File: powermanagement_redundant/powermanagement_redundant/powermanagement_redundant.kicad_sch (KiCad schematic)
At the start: 3 parts, among them K1 SISF00DN-T1-GE3, K2 SISF00DN-T1-GE3

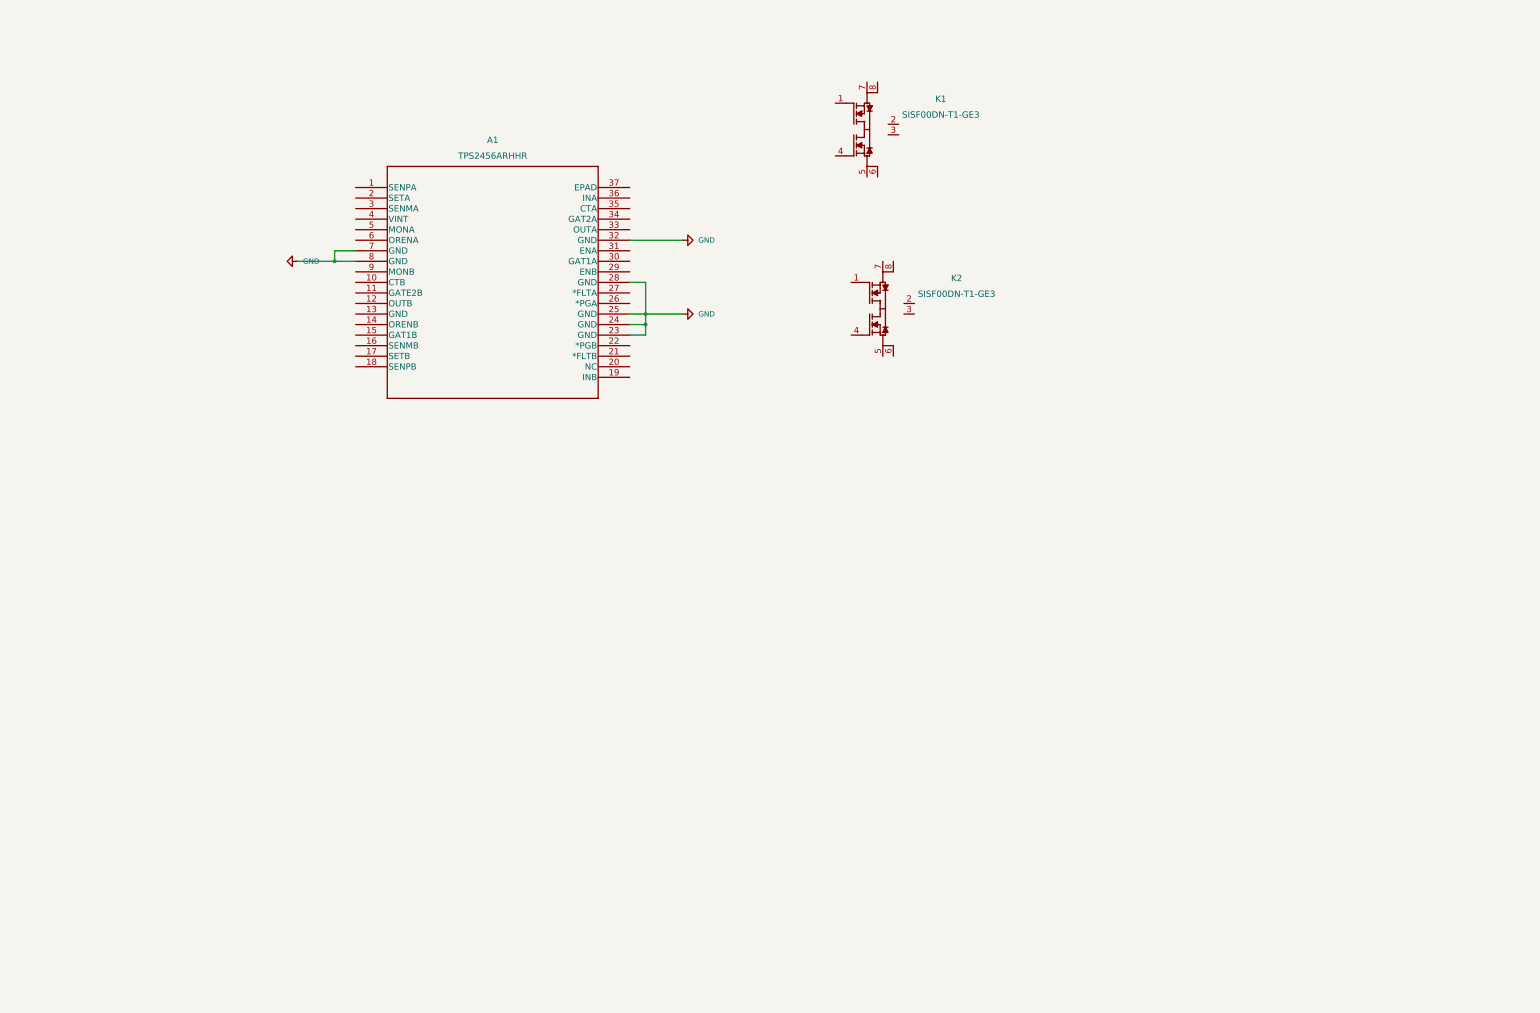
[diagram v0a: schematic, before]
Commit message: Bauteileplatzierung Fertig!
Alle Bauteile sind jetzt alle platziert. Werte die bereits Bekannt sind hab ich auch eingetragen. Berechnung der Bauteile erfolgt demnächst.
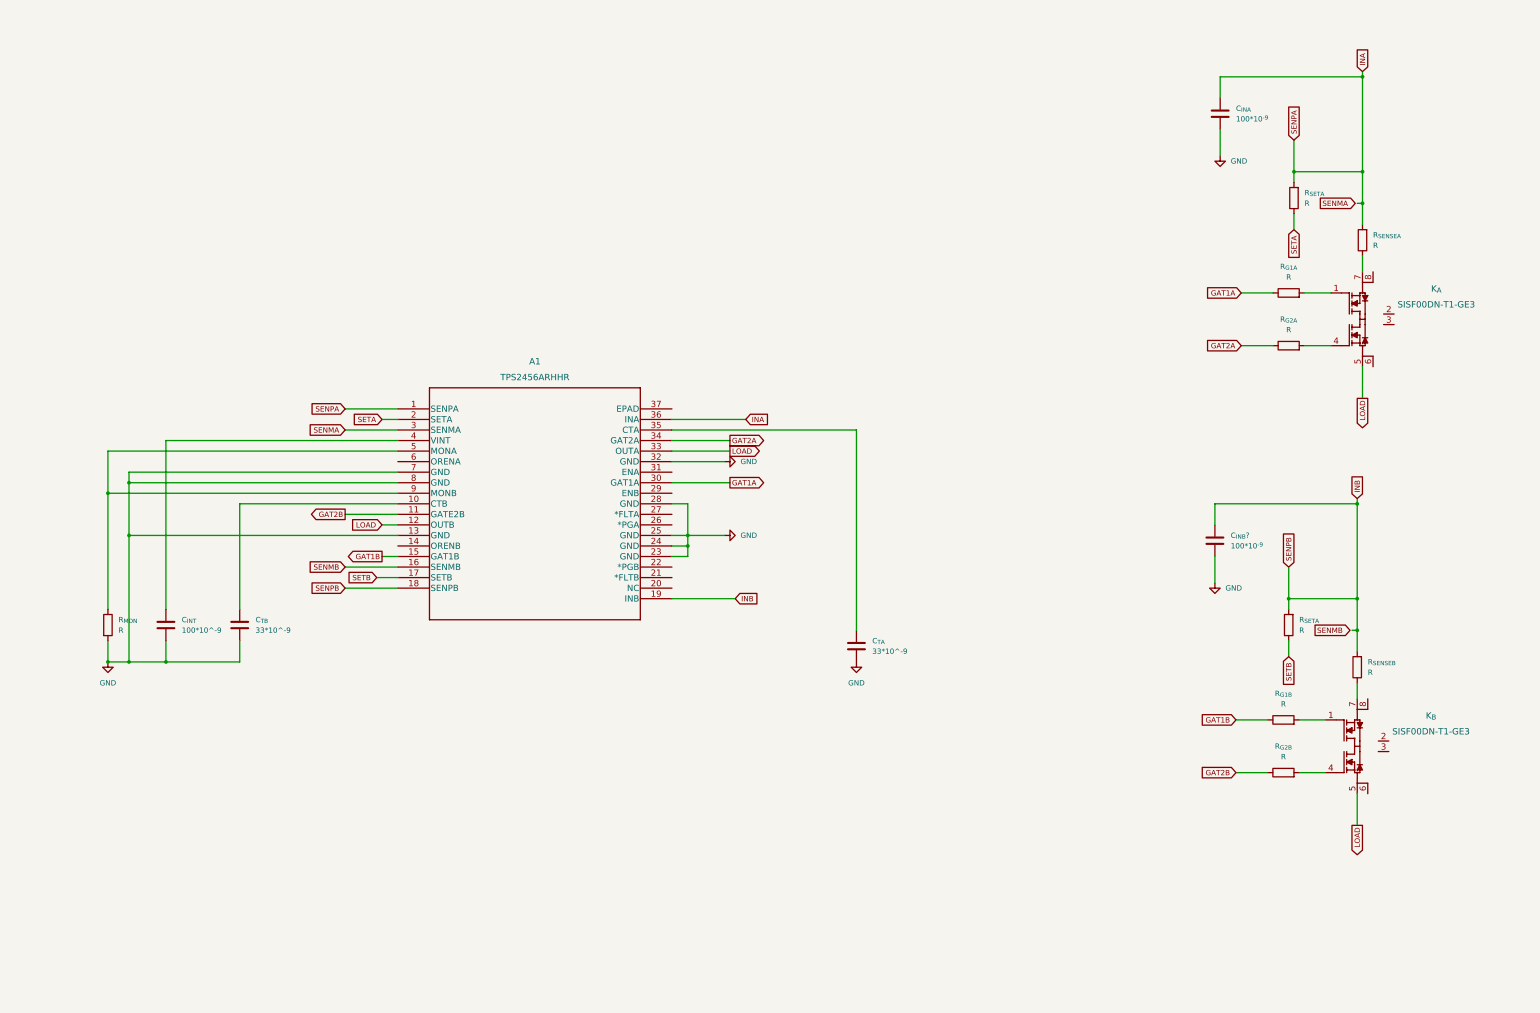
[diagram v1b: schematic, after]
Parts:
- removed K2: SISF00DN-T1-GE3, SISF00DN-1:SISF00DN-T1-GE3, symbol SISF00DN-T1:SISF00DN-T1-GE3
- added C_{INA}, C_{INB}?: 100*10^{-9}, symbol Device:C
- added C_{INT}: 100*10^-9, symbol Device:C
- added C_{TA}, C_{TB}: 33*10^-9, symbol Device:C
- added K_{B}: SISF00DN-T1-GE3, SISF00DN-1:SISF00DN-T1-GE3, symbol SISF00DN-T1:SISF00DN-T1-GE3
- added R_{G1A}, R_{G1B}, R_{G2A}, R_{G2B}, R_{MON}, R_{SENSEA}, R_{SENSEB}, R_{SETA} (x2): R, symbol Device:R
- renumbered K1 to K_{A}
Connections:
- net GND: now also A1.13 (GND), C_{INA}.2, C_{INB}?.2, C_{INT}.2, C_{TA}.2, C_{TB}.2, R_{MON}.2
- net at K_{A}.1 (G1): now also R_{G1A}.2
- net at K_{A}.4 (G2): now also R_{G2A}.2
- net LOAD: now reaches K_{A}.5 (S2)
- net LOAD: now also A1.12 (OUTB), A1.33 (OUTA), K_{B}.5 (S2)
- net at K_{A}.7 (S1): now also R_{SENSEA}.1
- net INA: now reaches A1.1 (SENPA)
- net INA: now also A1.36 (INA), C_{INA}.1, R_{SENSEA}.2, R_{SETA}.2
- net at A1.10 (CTB): now also C_{TB}.1
- net GAT2B: now reaches A1.11 (GATE2B)
- net GAT2B: now also R_{G2B}.1
- net GAT1B: now reaches A1.15 (GAT1B)
- net GAT1B: now also R_{G1B}.1
- net SENMB: now reaches A1.16 (SENMB)
- net SETB: now reaches A1.17 (SETB)
- net SETB: now also R_{SETA}.1
- net INB: now reaches A1.18 (SENPB)
- net INB: now also A1.19 (INB), C_{INB}?.1, R_{SENSEB}.2, R_{SETA}.2
- net SETA: now reaches A1.2 (SETA)
- net SETA: now also R_{SETA}.1
- net SENMA: now reaches A1.3 (SENMA)
- net GAT1A: now reaches A1.30 (GAT1A)
- net GAT1A: now also R_{G1A}.1
- net GAT2A: now reaches A1.34 (GAT2A)
- net GAT2A: now also R_{G2A}.1
- net at A1.35 (CTA): now also C_{TA}.1
- net at A1.4 (VINT): now also C_{INT}.1
- net at A1.5 (MONA): now also A1.9 (MONB), R_{MON}.1
- new net: K_{B}.1 (G1), R_{G1B}.2
- new net: K_{B}.4 (G2), R_{G2B}.2
- new net: K_{B}.7 (S1), R_{SENSEB}.1
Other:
- moved on the sheet: A1, K_{A}

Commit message: Komponenten finalisiert und ein wenig aufgeräumt
Den Schaltplan weitesgehen finalisiert.
PG und FLT LEDS hinzugefügt.
Fault clear Button hinzugefügt.
Wiederstände fürs current sensing berechnet.
Schaltplan aufgeräumt.
Soft turn on schaltung hinzugefügt
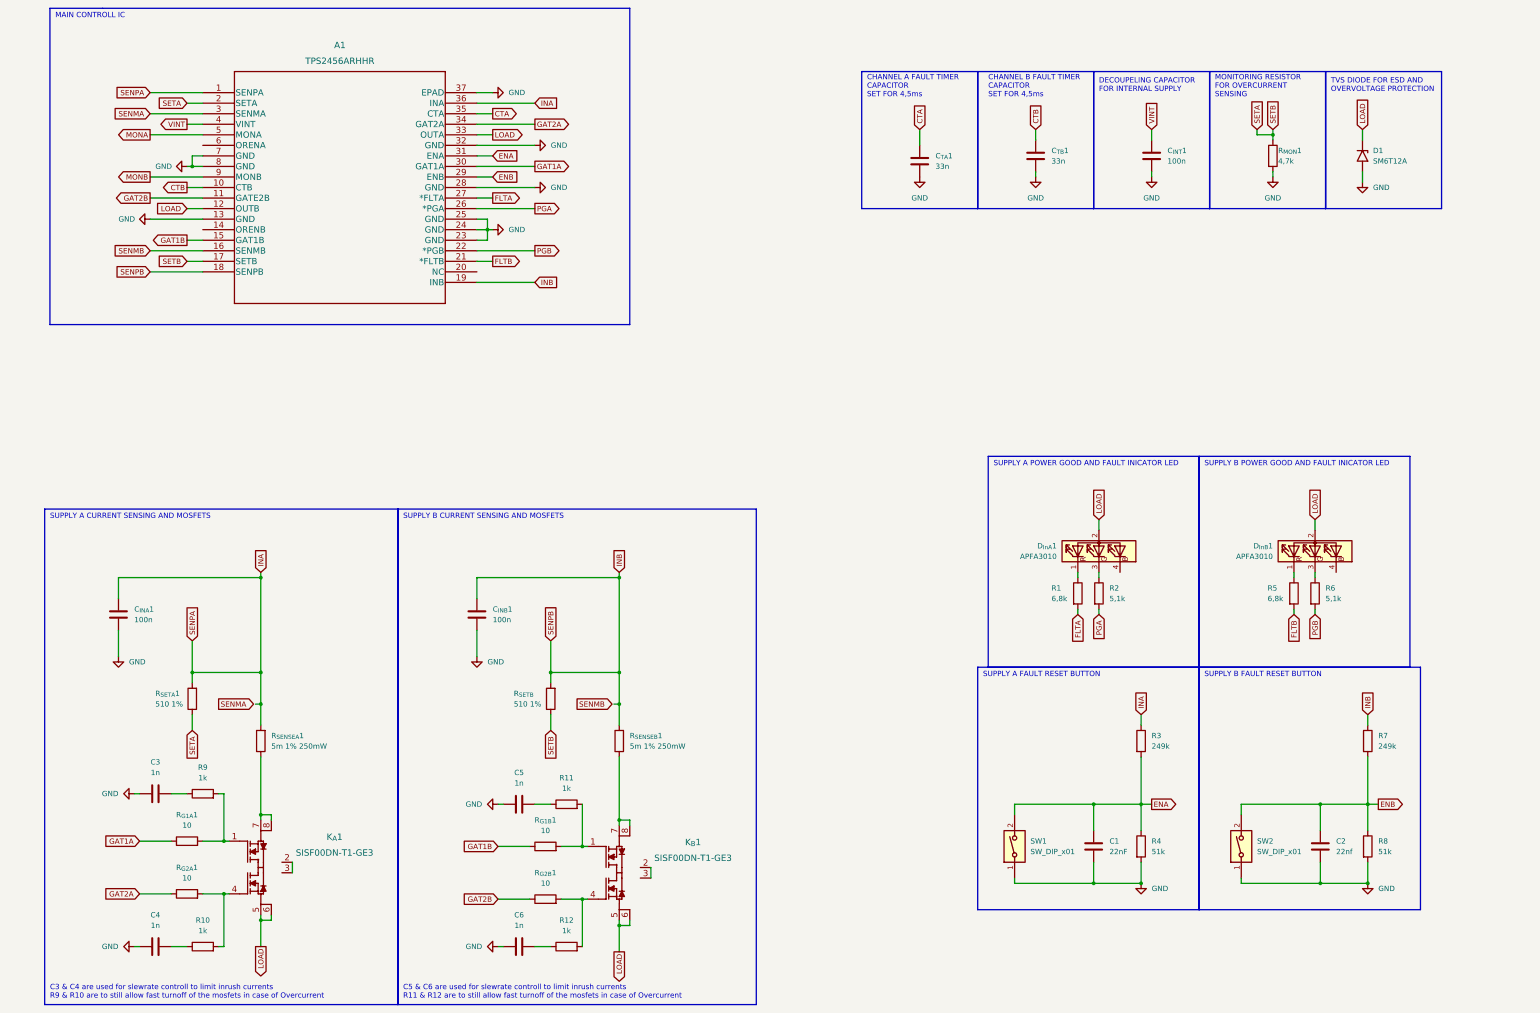
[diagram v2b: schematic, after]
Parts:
- added C1: 22nF, symbol Device:C
- added C2: 22nf, symbol Device:C
- added C3, C4, C5, C6: 1n, symbol Device:C
- added D1: SM6T12A, Diode_SMD:D_SMB, symbol Diode:SM6T12A
- added D_{InA}1, D_{InB}1: APFA3010, LED_SMD:LED_Kingbright_APFA3010_3x1.5mm_Horizontal, symbol LED:APFA3010
- added R1, R5: 6,8k, symbol Device:R
- added R10, R11, R12, R9: 1k, symbol Device:R
- added R2, R6: 5,1k, symbol Device:R
- added R3, R7: 249k, symbol Device:R
- added R4, R8: 51k, symbol Device:R
- added SW1, SW2: SW_DIP_x01, symbol Switch:SW_DIP_x01
- C_{INA}1: renamed from C_{INA}; value 100*10^{-9} -> 100n
- C_{INB}1: renamed from C_{INB}?; value 100*10^{-9} -> 100n
- C_{INT}1: renamed from C_{INT}; value 100*10^-9 -> 100n
- C_{TA}1: renamed from C_{TA}; value 33*10^-9 -> 33n
- C_{TB}1: renamed from C_{TB}; value 33*10^-9 -> 33n
- R_{G1A}1: renamed from R_{G1A}; value R -> 10
- R_{G1B}1: renamed from R_{G1B}; value R -> 10
- R_{G2A}1: renamed from R_{G2A}; value R -> 10
- R_{G2B}1: renamed from R_{G2B}; value R -> 10
- R_{MON}1: renamed from R_{MON}; value R -> 4,7k
- R_{SENSEA}1: renamed from R_{SENSEA}; value R -> 5m 1% 250mW; footprint (none) -> Resistor_SMD:R_0402_1005Metric_Pad0.72x0.64mm_HandSolder
- R_{SENSEB}1: renamed from R_{SENSEB}; value R -> 5m 1% 250mW; footprint (none) -> Resistor_SMD:R_0402_1005Metric_Pad0.72x0.64mm_HandSolder
- R_{SETA}1, R_{SETB}: renamed from R_{SETA}; value R -> 510 1%
- renumbered K_{A} to K_{A}1, K_{B} to K_{B}1
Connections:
- net SETB is gone; now on net SETA: A1.17 (SETB), R_{SETB}.1
- net GND: now also A1.37 (EPAD), C1.2, C2.2, C3.2, C4.2, C5.2, C6.2, D1.2 (A2), R4.2, R8.2, SW1.1, SW2.1
- net INA: now also R3.1
- net INB: now also R7.1
- net LOAD: now also K_{A}1.6 (S2), K_{B}1.6 (S2), D1.1 (A1), D_{InA}1.2 (A), D_{InB}1.2 (A)
- net SETA: now also R_{MON}1.1
- net at K_{B}1.1 (G1), R_{G1B}1.2: now also R11.2
- net at K_{A}1.1 (G1), R_{G1A}1.2: now also R9.2
- net at K_{A}1.2 (D1): now also K_{A}1.3 (D2)
- net at K_{A}1.4 (G2), R_{G2A}1.2: now also R10.2
- net at K_{A}1.7 (S1), R_{SENSEA}1.1: now also K_{A}1.8 (S1)
- net CTB: now reaches A1.10 (CTB), C_{TB}1.1
- net VINT: now reaches A1.4 (VINT), C_{INT}1.1
- net at K_{B}1.4 (G2), R_{G2B}1.2: now also R12.2
- net at K_{B}1.7 (S1), R_{SENSEB}1.1: now also K_{B}1.8 (S1)
- net FLTB: now reaches A1.21 (*FLTB)
- net FLTB: now also R5.2
- net PGB: now reaches A1.22 (*PGB)
- net PGB: now also R6.2
- net PGA: now reaches A1.26 (*PGA)
- net PGA: now also R2.2
- net FLTA: now reaches A1.27 (*FLTA)
- net FLTA: now also R1.2
- net ENB: now reaches A1.29 (ENB)
- net ENB: now also C2.1, R7.2, R8.1, SW2.2
- net ENA: now reaches A1.31 (ENA)
- net ENA: now also C1.1, R3.2, R4.1, SW1.2
- net CTA: now reaches A1.35 (CTA), C_{TA}1.1
- net at K_{B}1.2 (D1): now also K_{B}1.3 (D2)
- new net: D_{InB}1.1 (R), R5.1
- new net: D_{InB}1.3 (G), R6.1
- new net: C3.1, R9.1
- new net: C5.1, R11.1
- new net: C6.1, R12.1
- new net: C4.1, R10.1
- new net: D_{InA}1.1 (R), R1.1
- new net: D_{InA}1.3 (G), R2.1
- new net MONA: A1.5 (MONA)
- new net MONB: A1.9 (MONB)
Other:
- note added: "C3 & C4 are used for slewrate controll to limit inrush currents R9 & R10 are to still allow fast turnoff of the mosfets in case of Overcurrent"
- note added: "C5 & C6 are used for slewrate controll to limit inrush currents R11 & R12 are to still allow fast turnoff of the mosfets in case of Overcurrent"
- note added: "CHANNEL A FAULT TIMER CAPACITOR SET FOR 4,5ms"
- note added: "CHANNEL B FAULT TIMER CAPACITOR SET FOR 4,5ms"
- note added: "DECOUPELING CAPACITOR FOR INTERNAL SUPPLY"
- note added: "MAIN CONTROLL IC"
- note added: "MONITORING RESISTOR FOR OVERCURRENT SENSING"
- note added: "SUPPLY A CURRENT SENSING AND MOSFETS"
- note added: "SUPPLY A FAULT RESET BUTTON"
- note added: "SUPPLY A POWER GOOD AND FAULT INICATOR LED"
- note added: "SUPPLY B CURRENT SENSING AND MOSFETS"
- note added: "SUPPLY B FAULT RESET BUTTON"
- note added: "SUPPLY B POWER GOOD AND FAULT INICATOR LED"
- note added: "TVS DIODE FOR ESD AND OVERVOLTAGE PROTECTION"
- moved on the sheet: A1, C_{INA}1, C_{INB}1, C_{INT}1, C_{TA}1, C_{TB}1, K_{A}1, K_{B}1, R_{G1A}1, R_{G1B}1, R_{G2A}1, R_{G2B}1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

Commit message: Paar fehler gefixed und Footprints zugeordnet
Im Schaltplan noch ein paar fehler gefixed, Footprints zugeordnet und Komponenten rausgesucht.
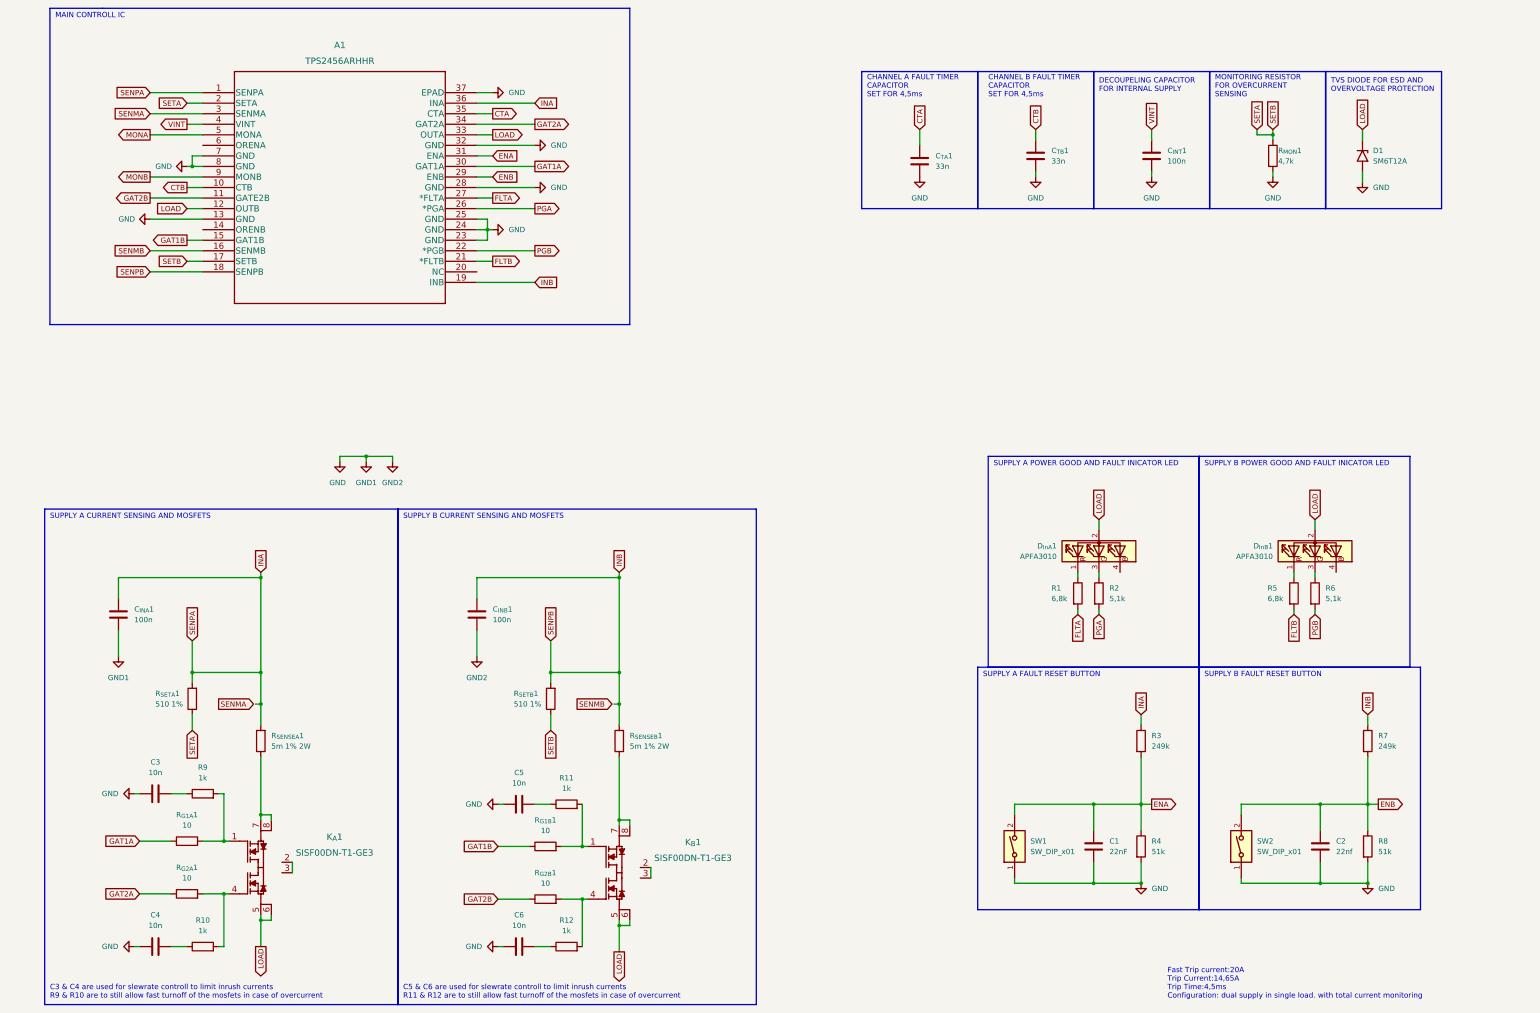
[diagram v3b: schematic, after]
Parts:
- C1, C2, C_{INA}1, C_{INB}1, C_{INT}1, C_{TA}1, C_{TB}1: footprint (none) -> Capacitor_SMD:C_0805_2012Metric_Pad1.18x1.45mm_HandSolder
- C3, C4, C5, C6: value 1n -> 10n; footprint (none) -> Capacitor_SMD:C_0805_2012Metric_Pad1.18x1.45mm_HandSolder
- R1, R10, R11, R12, R2, R3, R4, R5, R6, R7, R8, R9, R_{G1A}1, R_{G1B}1, R_{G2A}1, R_{G2B}1, R_{MON}1, R_{SETA}1: footprint (none) -> Resistor_SMD:R_0805_2012Metric_Pad1.20x1.40mm_HandSolder
- R_{SENSEA}1, R_{SENSEB}1: value 5m 1% 250mW -> 5m 1% 2W; footprint Resistor_SMD:R_0402_1005Metric_Pad0.72x0.64mm_HandSolder -> Resistor_SMD:R_0612_1632Metric_Pad1.18x3.40mm_HandSolder; Mouser Link (none) -> https://www.mouser.de/ProductDetail/Vishay/WFCP06125L000FE6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
- R_{SETB}1: renamed from R_{SETB}; footprint (none) -> Resistor_SMD:R_0805_2012Metric_Pad1.20x1.40mm_HandSolder
- SW1, SW2: footprint (none) -> Button_Switch_SMD:Panasonic_EVQPUL_EVQPUC; Name (none) -> EVQ-P7C01
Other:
- note added: "C3 & C4 are used for slewrate controll to limit inrush currents R9 & R10 are to still allow fast turnoff of the mosfets in case of overcurrent"
- note added: "C5 & C6 are used for slewrate controll to limit inrush currents R11 & R12 are to still allow fast turnoff of the mosfets in case of overcurrent"
- note added: "Fast Trip current:20A Trip Current:14,65A Trip Time:4,5ms Configuration: dual supply in single load. with total current monitoring"
- note removed: "C3 & C4 are used for slewrate controll to limit inrush currents R9 & R10 are to still allow fast turnoff of the mosfets in case of Overcurrent"
- note removed: "C5 & C6 are used for slewrate controll to limit inrush currents R11 & R12 are to still allow fast turnoff of the mosfets in case of Overcurrent"

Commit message: PCB angefangen
PCB halt angefangen
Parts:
- added J1, J2, J3, J4, J5, J6, J7, J8: Screw_Terminal_01x01, MountingHole:MountingHole_3.2mm_M3_Pad_Via, symbol Connector:Screw_Terminal_01x01
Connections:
- net GND: now also J3.1 (Pin_1), J4.1 (Pin_1), J7.1 (Pin_1), J8.1 (Pin_1)
- net INA: now also J1.1 (Pin_1), J2.1 (Pin_1)
- net INB: now also J5.1 (Pin_1), J6.1 (Pin_1)
